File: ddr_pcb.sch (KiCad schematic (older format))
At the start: 16 parts, among them J1 Screw_Terminal_01x04, J2 Screw_Terminal_01x04, J3 Screw_Terminal_01x04, J4 Screw_Terminal_01x06, J5 Screw_Terminal_01x04, U1 ProMicro

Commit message: new: Finished WIP
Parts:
- added 220ohm1: R_Small, Resistor_THT:R_Axial_DIN0204_L3.6mm_D1.6mm_P5.08mm_Horizontal, symbol Device:R_Small
- renumbered R6 to A0, R7 to A1, R5 to A10, R8 to A2, R9 to A3, R1 to A6, R2 to A7, R3 to A8, R4 to A9
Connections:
- net at U1.16 (B1): now also 220ohm1.2
- net at U1.23 (GND): now also J5.1 (Pin_1); no longer J5.3 (Pin_3)
- net at U1.8 (C6): no longer J5.2 (Pin_2)
- net at C1.2, J1.2 (Pin_2), J1.4 (Pin_4)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: now also J5.3 (Pin_3); no longer J5.1 (Pin_1)
- new net: 220ohm1.1, J5.2 (Pin_2)
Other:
- moved on the sheet: A0, A1, A10, A2, A3, A9

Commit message: new: Add text to silkscreen
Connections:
- net at C1.1, U1.21 (VCC): now also J1.2 (Pin_2), J1.4 (Pin_4), J2.2 (Pin_2), J2.4 (Pin_4), J3.2 (Pin_2), J3.4 (Pin_4), J4.2 (Pin_2), J4.4 (Pin_4), J4.6 (Pin_6)
- new net: C1.2, J5.3 (Pin_3)
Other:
- moved on the sheet: C1
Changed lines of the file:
@@
 L Device:CP C1
 U 1 1 6198070A
-P 4400 3350
-F 0 "C1" V 4655 3350 50  0000 C CNN
-F 1 "CP" V 4564 3350 50  0000 C CNN
-F 2 "Diode_THT:D_DO-34_SOD68_P10.16mm_Horizontal" H 4438 3200 50  0001 C CNN
-F 3 "~" H 4400 3350 50  0001 C CNN
-	1    4400 3350
+P 4400 3050
+F 0 "C1" V 4655 3050 50  0000 C CNN
+F 1 "CP" V 4564 3050 50  0000 C CNN
+F 2 "Diode_THT:D_DO-34_SOD68_P10.16mm_Horizontal" H 4438 2900 50  0001 C CNN
+F 3 "~" H 4400 3050 50  0001 C CNN
+	1    4400 3050
 	0    -1   -1   0
 $EndComp
-Wire Wire Line
-	4550 3350 4700 3350
 $Comp
 L Connector:Screw_Terminal_01x04 J5
@@
 	4050 2800 4350 2800
 Wire Wire Line
-	4700 3350 4700 2900
-Wire Wire Line
 	4700 2900 4950 2900
-Connection ~ 4700 3350
 Wire Wire Line
 	4150 2700 4950 2700
@@
 Wire Wire Line
 	1900 4200 1900 4400
+Wire Wire Line
+	4250 3050 4250 3350
+Wire Wire Line
+	4550 3050 4700 3050
+Wire Wire Line
+	4700 3050 4700 2900
+Wire Wire Line
+	4250 3350 4700 3350
+Connection ~ 4250 3350
 $EndSCHEMATC

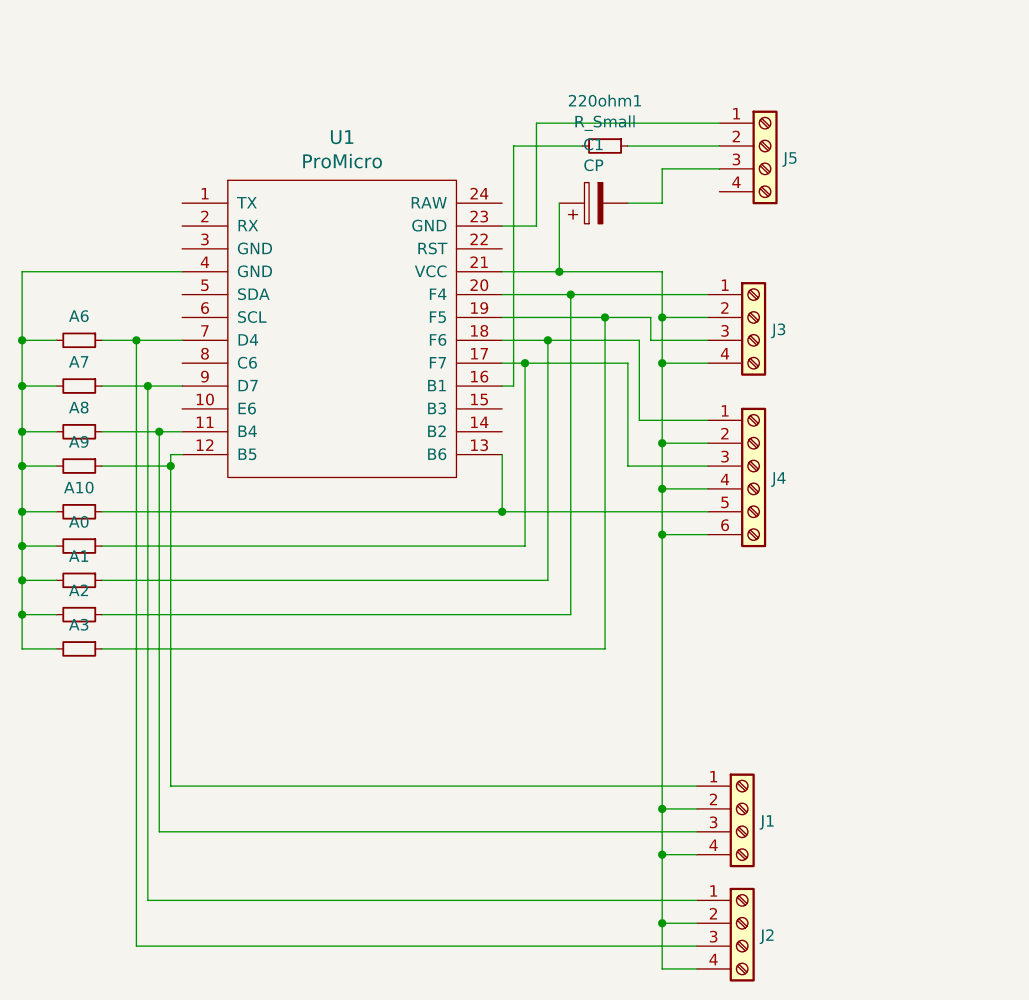
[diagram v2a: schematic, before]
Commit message: new: add bigger holes for resistors so that we can socket them
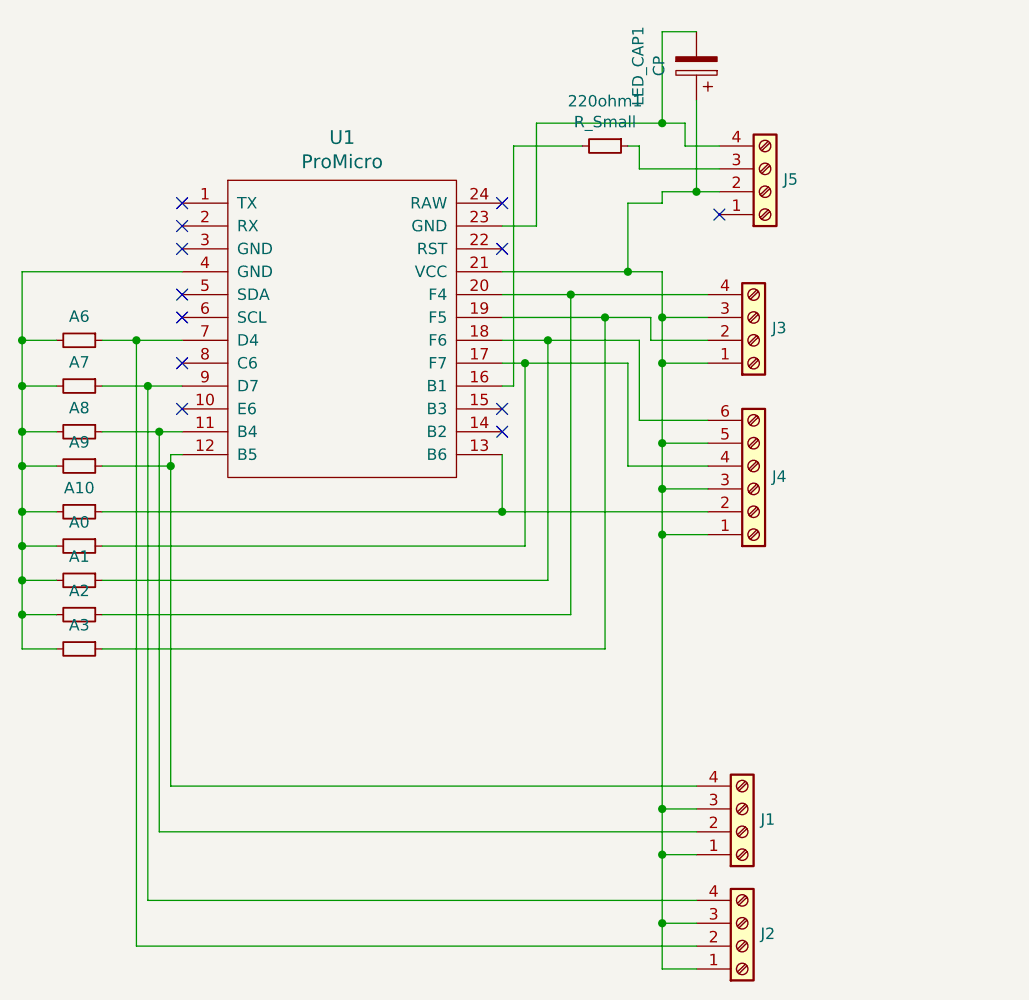
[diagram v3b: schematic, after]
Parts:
- J1, J2, J3, J5: footprint Connector_PinSocket_2.54mm:PinSocket_1x04_P2.54mm_Vertical -> TerminalBlock_Phoenix:TerminalBlock_Phoenix_MPT-0,5-4-2.54_1x04_P2.54mm_Horizontal
- J4: footprint Connector_PinSocket_2.54mm:PinSocket_1x06_P2.54mm_Vertical -> TerminalBlock_Phoenix:TerminalBlock_Phoenix_MPT-0,5-6-2.54_1x06_P2.54mm_Horizontal
- renumbered C1 to LED_CAP1
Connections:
- net at A8.1, U1.11 (B4): now also J1.2 (Pin_2); no longer J1.3 (Pin_3)
- net at A9.1, U1.12 (B5): now also J1.4 (Pin_4); no longer J1.1 (Pin_1)
- net at A10.1, U1.13 (B6): now also J4.2 (Pin_2); no longer J4.5 (Pin_5)
- net at A0.1, U1.17 (F7): now also J4.4 (Pin_4); no longer J4.3 (Pin_3)
- net at A1.1, U1.18 (F6): now also J4.6 (Pin_6); no longer J4.1 (Pin_1)
- net at A3.1, U1.19 (F5): now also J3.2 (Pin_2); no longer J3.3 (Pin_3)
- net at A2.1, U1.20 (F4): now also J3.4 (Pin_4); no longer J3.1 (Pin_1)
- net at U1.23 (GND): now also J5.4 (Pin_4), LED_CAP1.2; no longer J5.1 (Pin_1)
- net at A6.1, U1.7 (D4): now also J2.2 (Pin_2); no longer J2.3 (Pin_3)
- net at A7.1, U1.9 (D7): now also J2.4 (Pin_4); no longer J2.1 (Pin_1)
- net at J5.3 (Pin_3): now also 220ohm1.1; no longer LED_CAP1.2
- net at J5.2 (Pin_2): now also J1.1 (Pin_1), J1.3 (Pin_3), J2.1 (Pin_1), J2.3 (Pin_3), J3.1 (Pin_1), J3.3 (Pin_3), J4.1 (Pin_1), J4.3 (Pin_3), J4.5 (Pin_5), LED_CAP1.1, U1.21 (VCC); no longer 220ohm1.1
- no-connect marks 0 -> 12
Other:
- moved on the sheet: J5, LED_CAP1
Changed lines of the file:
@@
 L Connector:Screw_Terminal_01x04 J3
 U 1 1 6191BA8F
-P 5100 3550
-F 0 "J3" H 5180 3496 50  0000 L CNN
-F 1 "Screw_Terminal_01x04" H 5180 3451 50  0001 L CNN
-F 2 "Connector_PinSocket_2.54mm:PinSocket_1x04_P2.54mm_Vertical" H 5100 3550 50  0001 C CNN
-F 3 "~" H 5100 3550 50  0001 C CNN
-	1    5100 3550
-	1    0    0    -1
+P 5100 3650
+F 0 "J3" H 5180 3596 50  0000 L CNN
+F 1 "Screw_Terminal_01x04" H 5180 3551 50  0001 L CNN
+F 2 "TerminalBlock_Phoenix:TerminalBlock_Phoenix_MPT-0,5-4-2.54_1x04_P2.54mm_Horizontal" H 5100 3650 50  0001 C CNN
+F 3 "~" H 5100 3650 50  0001 C CNN
+	1    5100 3650
+	1    0    0    1
 $EndComp
 Wire Wire Line
@@
 L Connector:Screw_Terminal_01x06 J4
 U 1 1 619325E0
-P 5100 4200
-F 0 "J4" H 5180 4146 50  0000 L CNN
-F 1 "Screw_Terminal_01x06" H 5180 4101 50  0001 L CNN
-F 2 "Connector_PinSocket_2.54mm:PinSocket_1x06_P2.54mm_Vertical" H 5100 4200 50  0001 C CNN
-F 3 "~" H 5100 4200 50  0001 C CNN
-	1    5100 4200
-	1    0    0    -1
+P 5100 4300
+F 0 "J4" H 5180 4246 50  0000 L CNN
+F 1 "Screw_Terminal_01x06" H 5180 4201 50  0001 L CNN
+F 2 "TerminalBlock_Phoenix:TerminalBlock_Phoenix_MPT-0,5-6-2.54_1x06_P2.54mm_Horizontal" H 5100 4300 50  0001 C CNN
+F 3 "~" H 5100 4300 50  0001 C CNN
+	1    5100 4300
+	1    0    0    1
 $EndComp
 Wire Wire Line
@@
 L Connector:Screw_Terminal_01x04 J1
 U 1 1 61936B01
-P 5050 5700
-F 0 "J1" H 5130 5646 50  0000 L CNN
-F 1 "Screw_Terminal_01x04" H 5130 5601 50  0001 L CNN
-F 2 "Connector_PinSocket_2.54mm:PinSocket_1x04_P2.54mm_Vertical" H 5050 5700 50  0001 C CNN
-F 3 "~" H 5050 5700 50  0001 C CNN
-	1    5050 5700
-	1    0    0    -1
+P 5050 5800
+F 0 "J1" H 5130 5746 50  0000 L CNN
+F 1 "Screw_Terminal_01x04" H 5130 5701 50  0001 L CNN
+F 2 "TerminalBlock_Phoenix:TerminalBlock_Phoenix_MPT-0,5-4-2.54_1x04_P2.54mm_Horizontal" H 5050 5800 50  0001 C CNN
+F 3 "~" H 5050 5800 50  0001 C CNN
+	1    5050 5800
+	1    0    0    1
 $EndComp
 $Comp
 L Connector:Screw_Terminal_01x04 J2
 U 1 1 61938213
-P 5050 6200
-F 0 "J2" H 5130 6146 50  0000 L CNN
-F 1 "Screw_Terminal_01x04" H 5130 6101 50  0001 L CNN
-F 2 "Connector_PinSocket_2.54mm:PinSocket_1x04_P2.54mm_Vertical" H 5050 6200 50  0001 C CNN
-F 3 "~" H 5050 6200 50  0001 C CNN
-	1    5050 6200
-	1    0    0    -1
-$EndComp
-Wire Wire Line
-	4000 3350 4250 3350
+P 5050 6300
+F 0 "J2" H 5130 6246 50  0000 L CNN
+F 1 "Screw_Terminal_01x04" H 5130 6201 50  0001 L CNN
+F 2 "TerminalBlock_Phoenix:TerminalBlock_Phoenix_MPT-0,5-4-2.54_1x04_P2.54mm_Horizontal" H 5050 6300 50  0001 C CNN
+F 3 "~" H 5050 6300 50  0001 C CNN
+	1    5050 6300
+	1    0    0    1
+$EndComp
 Wire Wire Line
 	4700 3350 4700 3550
@@
 $EndComp
 $Comp
-L Device:CP C1
+L Device:CP LED_CAP1
 U 1 1 6198070A
-P 4400 3050
-F 0 "C1" V 4655 3050 50  0000 C CNN
-F 1 "CP" V 4564 3050 50  0000 C CNN
-F 2 "Diode_THT:D_DO-34_SOD68_P10.16mm_Horizontal" H 4438 2900 50  0001 C CNN
-F 3 "~" H 4400 3050 50  0001 C CNN
-	1    4400 3050
-	0    -1   -1   0
-$EndComp
-$Comp
-L Connector:Screw_Terminal_01x04 J5
-U 1 1 61985061
-P 5150 2800
-F 0 "J5" H 5230 2746 50  0000 L CNN
-F 1 "Screw_Terminal_01x04" H 5230 2701 50  0001 L CNN
-F 2 "Connector_PinSocket_2.54mm:PinSocket_1x04_P2.54mm_Vertical" H 5150 2800 50  0001 C CNN
-F 3 "~" H 5150 2800 50  0001 C CNN
-	1    5150 2800
-	1    0    0    -1
+P 4850 2450
+F 0 "LED_CAP1" V 5105 2450 50  0000 C CNN
+F 1 "CP" V 5014 2450 50  0000 C CNN
+F 2 "Diode_THT:D_DO-34_SOD68_P10.16mm_Horizontal" H 4888 2300 50  0001 C CNN
+F 3 "~" H 4850 2450 50  0001 C CNN
+	1    4850 2450
+	-1   0    0    1
 $EndComp
 Wire Wire Line
@@
 Wire Wire Line
 	4050 2800 4350 2800
-Wire Wire Line
-	4700 2900 4950 2900
-Wire Wire Line
-	4150 2700 4950 2700
 Wire Wire Line
 	4150 2700 4150 3150
@@
 $EndComp
 Wire Wire Line
-	4550 2800 4950 2800
-Wire Wire Line
 	4000 4400 2250 4400
 Connection ~ 4000 4400
@@
 	1900 4200 1900 4400
 Wire Wire Line
-	4250 3050 4250 3350
-Wire Wire Line
 	4550 3050 4700 3050
 Wire Wire Line
-	4700 3050 4700 2900
-Wire Wire Line
-	4250 3350 4700 3350
-Connection ~ 4250 3350
+	4550 2800 4600 2800
+Wire Wire Line
+	4600 2800 4600 2900
+Wire Wire Line
+	4600 2900 4950 2900
+$Comp
+L Connector:Screw_Terminal_01x04 J5
+U 1 1 61985061
+P 5150 3000
+F 0 "J5" H 5230 2946 50  0000 L CNN
+F 1 "Screw_Terminal_01x04" H 5230 2901 50  0001 L CNN
+F 2 "TerminalBlock_Phoenix:TerminalBlock_Phoenix_MPT-0,5-4-2.54_1x04_P2.54mm_Horizontal" H 5150 3000 50  0001 C CNN
+F 3 "~" H 5150 3000 50  0001 C CNN
+	1    5150 3000
+	1    0    0    1
+$EndComp
+Wire Wire Line
+	4700 3050 4700 3000
+Wire Wire Line
+	4700 3000 4850 3000
+Wire Wire Line
+	4800 2700 4800 2800
+Wire Wire Line
+	4800 2800 4950 2800
+Wire Wire Line
+	4550 3050 4550 3350
+Connection ~ 4550 3350
+Wire Wire Line
+	4550 3350 4700 3350
+Wire Wire Line
+	4150 2700 4700 2700
+Wire Wire Line
+	4000 3350 4550 3350
+Wire Wire Line
+	4850 3000 4850 2600
+Connection ~ 4850 3000
+Wire Wire Line
+	4850 3000 4950 3000
+Wire Wire Line
+	4700 2700 4700 2300
+Wire Wire Line
+	4700 2300 4850 2300
+Connection ~ 4700 2700
+Wire Wire Line
+	4700 2700 4800 2700
+NoConn ~ 2600 3750
+NoConn ~ 2600 3950
+NoConn ~ 2600 3550
+NoConn ~ 2600 3450
+NoConn ~ 2600 3250
+NoConn ~ 2600 3150
+NoConn ~ 2600 3050
+NoConn ~ 4000 3050
+NoConn ~ 4000 3250
+NoConn ~ 4000 3950
+NoConn ~ 4000 4050
+NoConn ~ 4950 3100
 $EndSCHEMATC

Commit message: Change resistor to have a bigger hole, fix text size
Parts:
- 220ohm1: footprint Resistor_THT:R_Axial_DIN0204_L3.6mm_D1.6mm_P5.08mm_Horizontal -> ddr_pcb:R_Axial_DDRPAD_L3.6mm_D1.6mm_P7.62mm_Horizontal
- A0, A1, A10, A2, A3, A6, A7, A8, A9: footprint Resistor_THT:R_Axial_DIN0204_L3.6mm_D1.6mm_P7.62mm_Horizontal -> ddr_pcb:R_Axial_DDRPAD_L3.6mm_D1.6mm_P7.62mm_Horizontal
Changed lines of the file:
@@
 F 0 "A6" V 2046 3650 50  0000 C CNN
 F 1 "R_Small" V 2045 3650 50  0001 C CNN
-F 2 "Resistor_THT:R_Axial_DIN0204_L3.6mm_D1.6mm_P7.62mm_Horizontal" H 2150 3650 50  0001 C CNN
+F 2 "ddr_pcb:R_Axial_DDRPAD_L3.6mm_D1.6mm_P7.62mm_Horizontal" H 2150 3650 50  0001 C CNN
 F 3 "~" H 2150 3650 50  0001 C CNN
 	1    2150 3650
@@
 F 0 "A7" V 2046 3850 50  0000 C CNN
 F 1 "R_Small" V 2045 3850 50  0001 C CNN
-F 2 "Resistor_THT:R_Axial_DIN0204_L3.6mm_D1.6mm_P7.62mm_Horizontal" H 2150 3850 50  0001 C CNN
+F 2 "ddr_pcb:R_Axial_DDRPAD_L3.6mm_D1.6mm_P7.62mm_Horizontal" H 2150 3850 50  0001 C CNN
 F 3 "~" H 2150 3850 50  0001 C CNN
 	1    2150 3850
@@
 F 0 "A8" V 2046 4050 50  0000 C CNN
 F 1 "R_Small" V 2045 4050 50  0001 C CNN
-F 2 "Resistor_THT:R_Axial_DIN0204_L3.6mm_D1.6mm_P7.62mm_Horizontal" H 2150 4050 50  0001 C CNN
+F 2 "ddr_pcb:R_Axial_DDRPAD_L3.6mm_D1.6mm_P7.62mm_Horizontal" H 2150 4050 50  0001 C CNN
 F 3 "~" H 2150 4050 50  0001 C CNN
 	1    2150 4050
@@
 F 0 "A9" V 2046 4200 50  0000 C CNN
 F 1 "R_Small" V 2045 4200 50  0001 C CNN
-F 2 "Resistor_THT:R_Axial_DIN0204_L3.6mm_D1.6mm_P7.62mm_Horizontal" H 2150 4200 50  0001 C CNN
+F 2 "ddr_pcb:R_Axial_DDRPAD_L3.6mm_D1.6mm_P7.62mm_Horizontal" H 2150 4200 50  0001 C CNN
 F 3 "~" H 2150 4200 50  0001 C CNN
 	1    2150 4200
@@
 F 0 "A10" V 2046 4400 50  0000 C CNN
 F 1 "R_Small" V 2045 4400 50  0001 C CNN
-F 2 "Resistor_THT:R_Axial_DIN0204_L3.6mm_D1.6mm_P7.62mm_Horizontal" H 2150 4400 50  0001 C CNN
+F 2 "ddr_pcb:R_Axial_DDRPAD_L3.6mm_D1.6mm_P7.62mm_Horizontal" H 2150 4400 50  0001 C CNN
 F 3 "~" H 2150 4400 50  0001 C CNN
 	1    2150 4400
@@
 F 0 "A0" V 2046 4550 50  0000 C CNN
 F 1 "R_Small" V 2045 4550 50  0001 C CNN
-F 2 "Resistor_THT:R_Axial_DIN0204_L3.6mm_D1.6mm_P7.62mm_Horizontal" H 2150 4550 50  0001 C CNN
+F 2 "ddr_pcb:R_Axial_DDRPAD_L3.6mm_D1.6mm_P7.62mm_Horizontal" H 2150 4550 50  0001 C CNN
 F 3 "~" H 2150 4550 50  0001 C CNN
 	1    2150 4550
@@
 F 0 "A1" V 2046 4700 50  0000 C CNN
 F 1 "R_Small" V 2045 4700 50  0001 C CNN
-F 2 "Resistor_THT:R_Axial_DIN0204_L3.6mm_D1.6mm_P7.62mm_Horizontal" H 2150 4700 50  0001 C CNN
+F 2 "ddr_pcb:R_Axial_DDRPAD_L3.6mm_D1.6mm_P7.62mm_Horizontal" H 2150 4700 50  0001 C CNN
 F 3 "~" H 2150 4700 50  0001 C CNN
 	1    2150 4700
@@
 F 0 "A2" V 2046 4850 50  0000 C CNN
 F 1 "R_Small" V 2045 4850 50  0001 C CNN
-F 2 "Resistor_THT:R_Axial_DIN0204_L3.6mm_D1.6mm_P7.62mm_Horizontal" H 2150 4850 50  0001 C CNN
+F 2 "ddr_pcb:R_Axial_DDRPAD_L3.6mm_D1.6mm_P7.62mm_Horizontal" H 2150 4850 50  0001 C CNN
 F 3 "~" H 2150 4850 50  0001 C CNN
 	1    2150 4850
@@
 F 0 "A3" V 2046 5000 50  0000 C CNN
 F 1 "R_Small" V 2045 5000 50  0001 C CNN
-F 2 "Resistor_THT:R_Axial_DIN0204_L3.6mm_D1.6mm_P7.62mm_Horizontal" H 2150 5000 50  0001 C CNN
+F 2 "ddr_pcb:R_Axial_DDRPAD_L3.6mm_D1.6mm_P7.62mm_Horizontal" H 2150 5000 50  0001 C CNN
 F 3 "~" H 2150 5000 50  0001 C CNN
 	1    2150 5000
@@
 F 0 "220ohm1" V 4254 2800 50  0000 C CNN
 F 1 "R_Small" V 4345 2800 50  0000 C CNN
-F 2 "Resistor_THT:R_Axial_DIN0204_L3.6mm_D1.6mm_P5.08mm_Horizontal" H 4450 2800 50  0001 C CNN
+F 2 "ddr_pcb:R_Axial_DDRPAD_L3.6mm_D1.6mm_P7.62mm_Horizontal" H 4450 2800 50  0001 C CNN
 F 3 "~" H 4450 2800 50  0001 C CNN
 	1    4450 2800

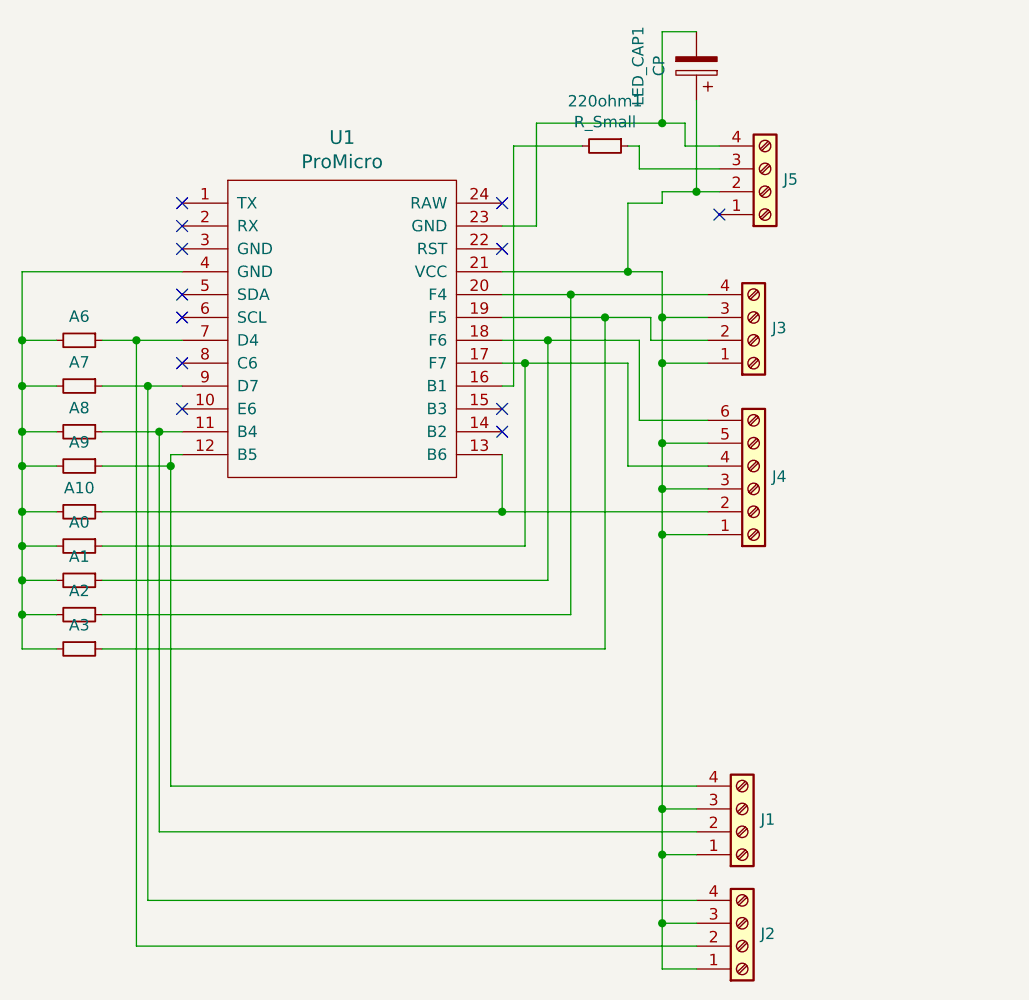
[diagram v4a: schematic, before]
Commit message: new: Add extra link for APA102
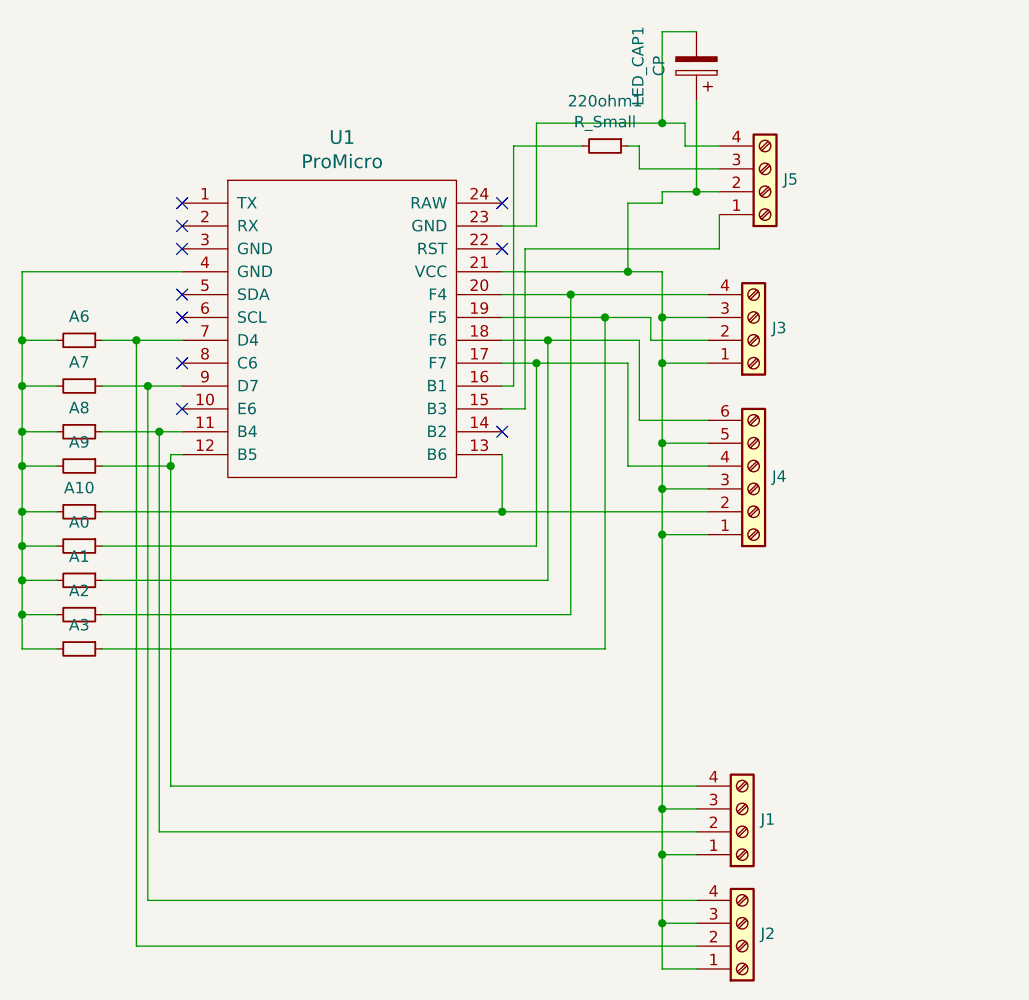
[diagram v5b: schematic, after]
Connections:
- net at U1.15 (B3): now also J5.1 (Pin_1)
- no-connect marks 12 -> 10
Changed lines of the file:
@@
 	4000 3650 4200 3650
-Wire Wire Line
-	4000 3750 4100 3750
-Wire Wire Line
-	4100 3750 4100 4550
 Wire Wire Line
 	4200 3650 4200 4700
@@
 Connection ~ 4200 3650
 Wire Wire Line
-	4100 3750 4550 3750
-Wire Wire Line
 	4550 3750 4550 4200
 Wire Wire Line
 	4550 4200 4900 4200
-Connection ~ 4100 3750
 Wire Wire Line
 	4000 4400 4900 4400
@@
 Wire Wire Line
 	2050 4700 1900 4700
-Wire Wire Line
-	2250 4550 4100 4550
 Wire Wire Line
 	1900 4050 1900 4200
@@
 NoConn ~ 4000 3050
 NoConn ~ 4000 3250
-NoConn ~ 4000 3950
 NoConn ~ 4000 4050
-NoConn ~ 4950 3100
+Wire Wire Line
+	4000 3750 4150 3750
+Connection ~ 4150 3750
+Wire Wire Line
+	4150 3750 4550 3750
+Wire Wire Line
+	4150 3750 4150 4550
+Wire Wire Line
+	2250 4550 4150 4550
+Wire Wire Line
+	4000 3950 4100 3950
+Wire Wire Line
+	4100 3950 4100 3250
+Wire Wire Line
+	4100 3250 4950 3250
+Wire Wire Line
+	4950 3250 4950 3100
 $EndSCHEMATC
